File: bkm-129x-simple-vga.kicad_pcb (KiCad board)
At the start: 2 copper layers, 105 x 89.3 mm, 55 parts, among them J1 DB15_Female_HighDensity_Mount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, J5 Conn_02x32_Row_Letter_Last, Q1 DTC144EKA, Q2 MMBT3904, SW1 PBH4UEENAGX, U1 ADG1611, U2 THS7374, U3 arduino-nano-v3, U4 74LVC125, U5 MIC3490-3.3

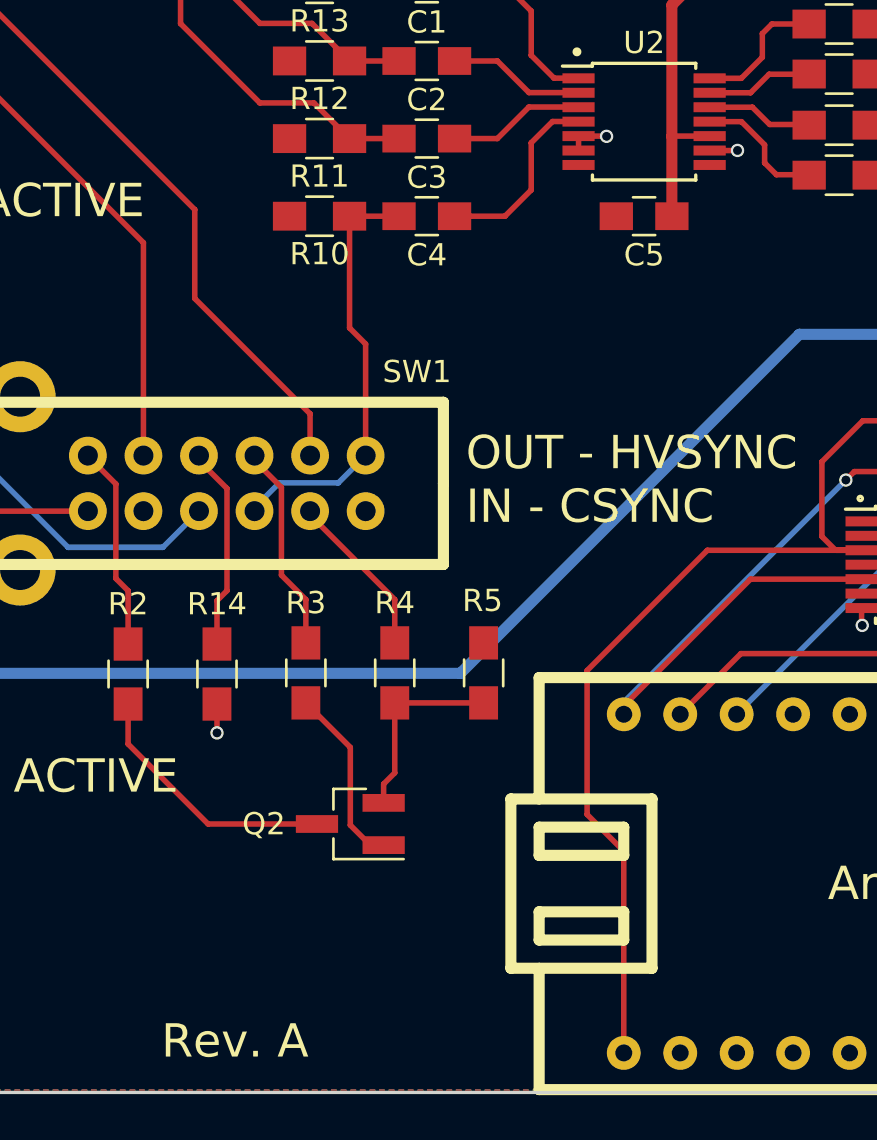
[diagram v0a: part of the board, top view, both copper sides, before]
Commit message: Rev. B: Fix THS7374, VGA pin 9, Kicad 5
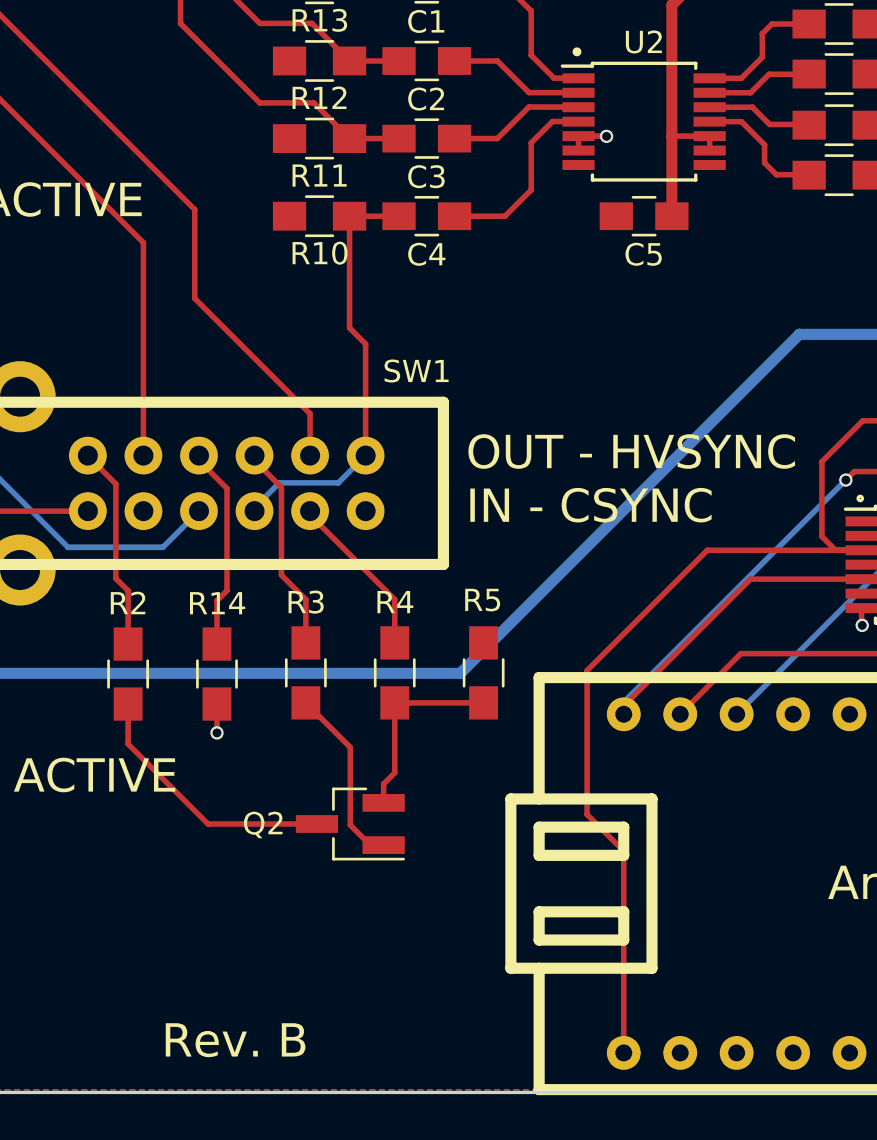
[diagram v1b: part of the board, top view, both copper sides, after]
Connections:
- J1 pad 9: GND -> (no net)
- U2 pad 9: GND -> +3V3
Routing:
- net GND: track 12.0 -> 10.7 mm, vias 9 -> 8
- net +3V3: track 16.0 -> 16.7 mm
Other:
- rule pad_to_mask_clearance: 0.2 -> 0
- board text added: "Rev. B"
- board text removed: "Rev. A"
